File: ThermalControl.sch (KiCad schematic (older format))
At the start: 19 parts, among them U1 ADA4528-2ACPZ-RL, U2 ADA4528-2ACPZ-RL

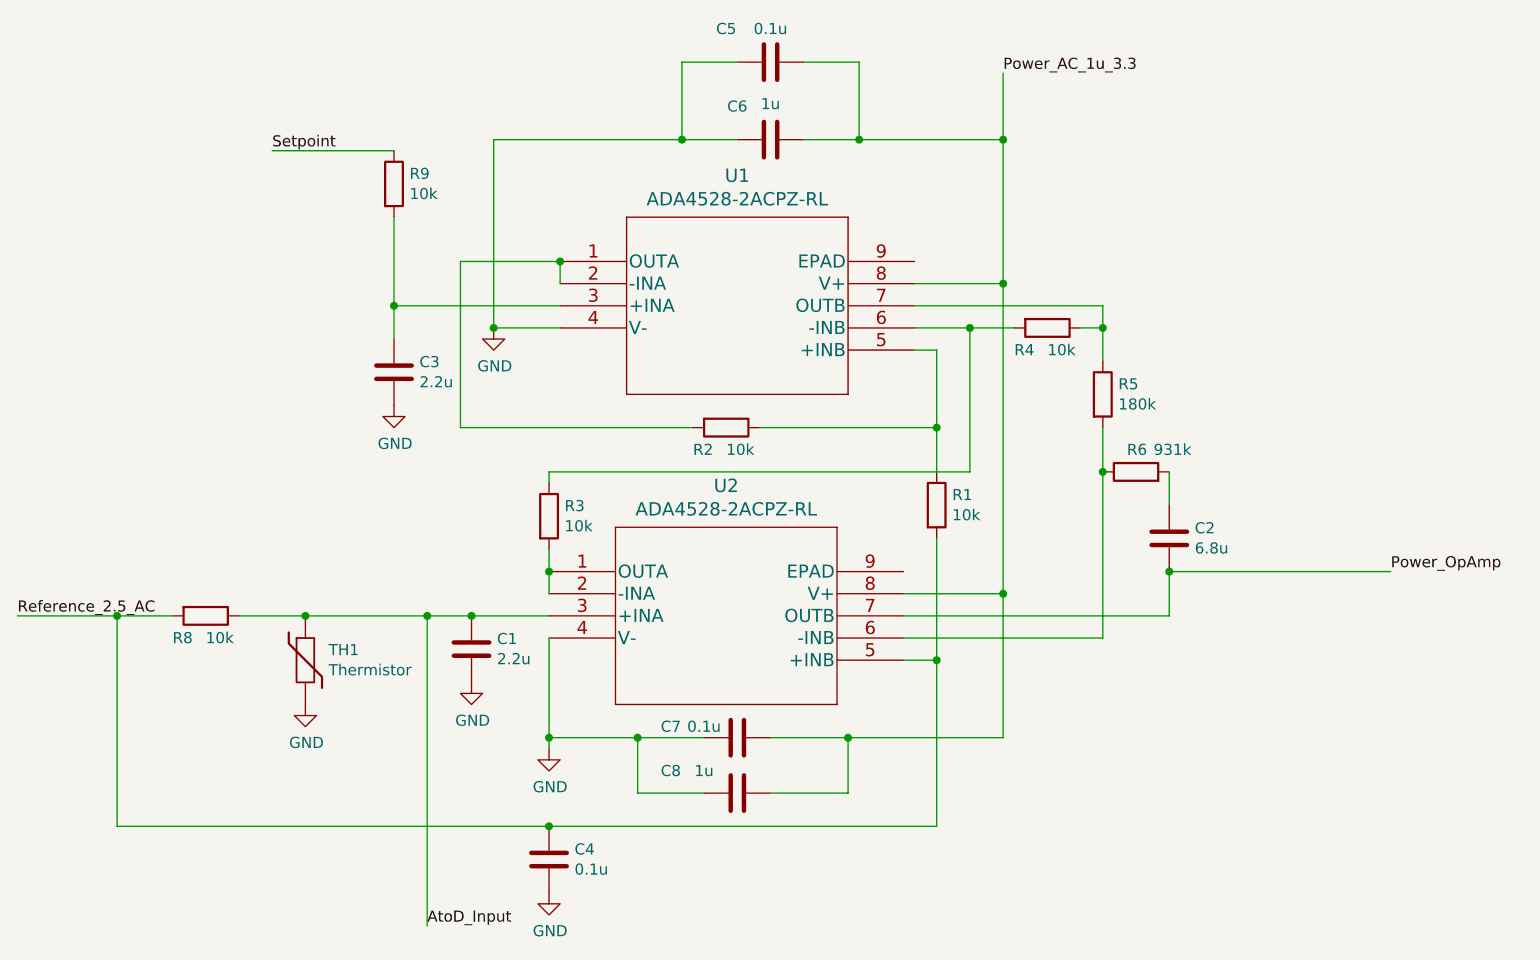
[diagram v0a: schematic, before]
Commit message: annotate all sheets
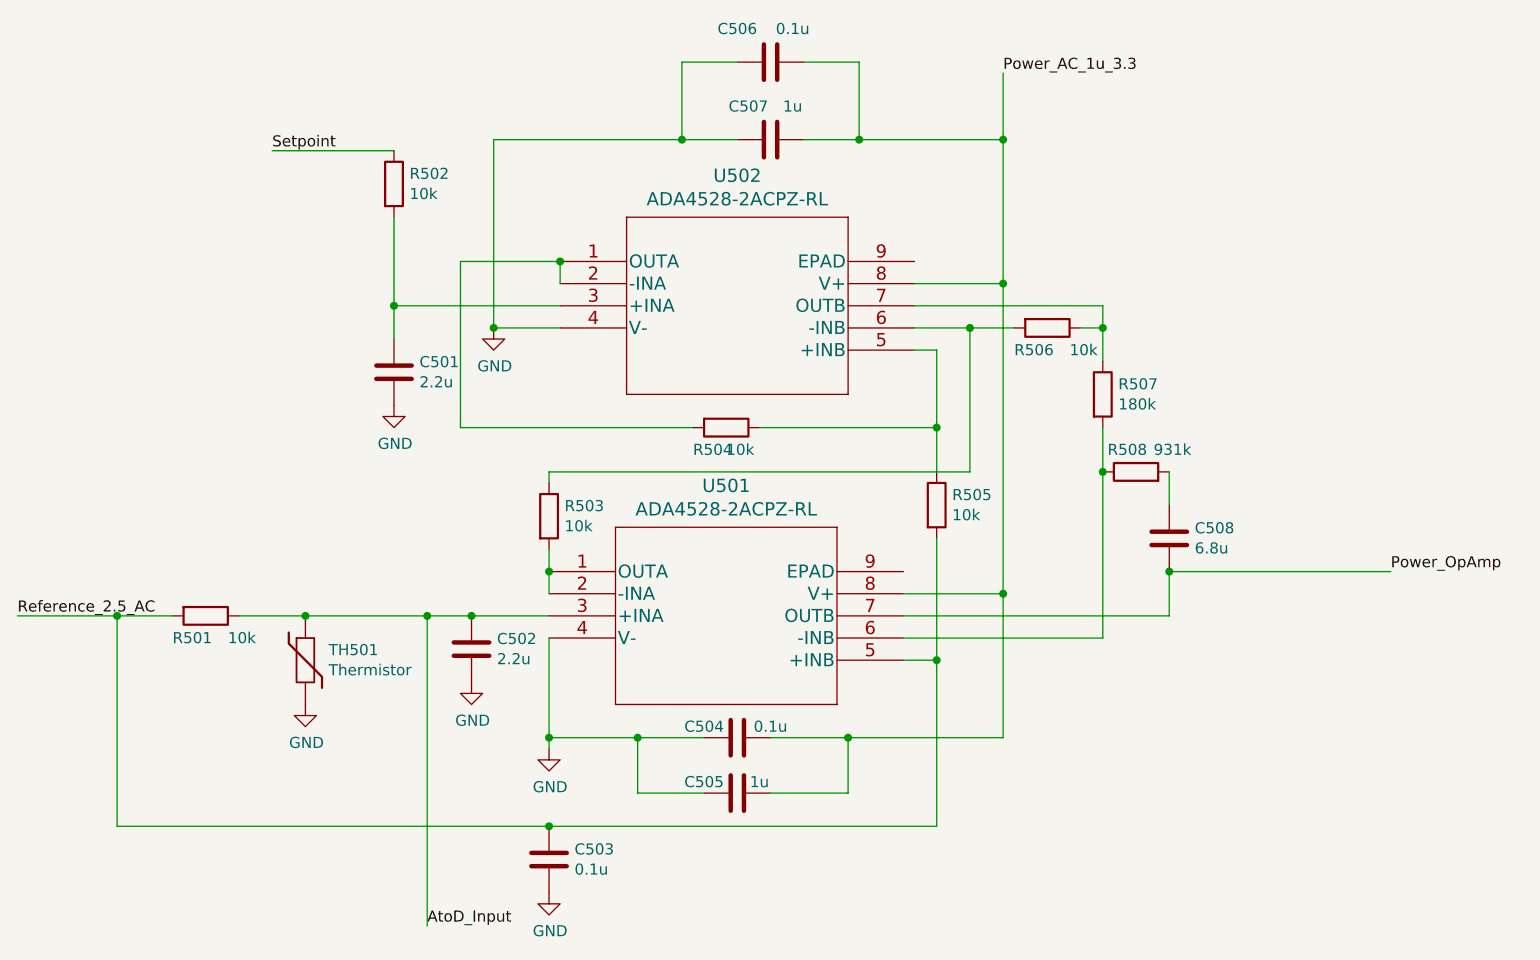
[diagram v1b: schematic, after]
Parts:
- renumbered C3 to C501, C1 to C502, C4 to C503, C7 to C504, C8 to C505, C5 to C506, C6 to C507, C2 to C508, R8 to R501, R9 to R502, R3 to R503, R2 to R504, R1 to R505, R4 to R506, R5 to R507, R6 to R508, TH1 to TH501, U2 to U501, U1 to U502
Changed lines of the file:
@@
 $EndDescr
 $Comp
-L ADA4528-2ACPZ-RL:ADA4528-2ACPZ-RL U2
+L ADA4528-2ACPZ-RL:ADA4528-2ACPZ-RL U501
 U 1 1 60C2B7EB
 P 4800 4550
-F 0 "U2" H 5600 4937 60  0000 C CNN
+F 0 "U501" H 5600 4937 60  0000 C CNN
 F 1 "ADA4528-2ACPZ-RL" H 5600 4831 60  0000 C CNN
 F 2 "CP_8_11_ADI" H 5600 4790 60  0001 C CNN
@@
 $EndComp
 $Comp
-L Device:R R9
+L Device:R R502
 U 1 1 60C2E3AF
 P 4100 2800
-F 0 "R9" H 4170 2846 50  0000 L CNN
+F 0 "R502" H 4170 2846 50  0000 L CNN
 F 1 "10k" H 4170 2755 50  0000 L CNN
 F 2 "" V 4030 2800 50  0001 C CNN
@@
 $EndComp
 $Comp
-L Device:R R4
+L Device:R R506
 U 1 1 60C2E585
 P 7050 3450
-F 0 "R4" V 7150 3300 50  0000 L CNN
-F 1 "10k" V 7150 3450 50  0000 L CNN
+F 0 "R506" V 7150 3300 50  0000 L CNN
+F 1 "10k" V 7150 3550 50  0000 L CNN
 F 2 "" V 6980 3450 50  0001 C CNN
 F 3 "~" H 7050 3450 50  0001 C CNN
@@
 $EndComp
 $Comp
-L Device:R R2
+L Device:R R504
 U 1 1 60C2FA14
 P 5600 3900
-F 0 "R2" V 5700 3750 50  0000 L CNN
+F 0 "R504" V 5700 3750 50  0000 L CNN
 F 1 "10k" V 5700 3900 50  0000 L CNN
 F 2 "" V 5530 3900 50  0001 C CNN
@@
 $EndComp
 $Comp
-L Device:R R5
+L Device:R R507
 U 1 1 60C30AE7
 P 7300 3750
-F 0 "R5" H 7370 3796 50  0000 L CNN
+F 0 "R507" H 7370 3796 50  0000 L CNN
 F 1 "180k" H 7370 3705 50  0000 L CNN
 F 2 "" V 7230 3750 50  0001 C CNN
@@
 $EndComp
 $Comp
-L Device:R R6
+L Device:R R508
 U 1 1 60C314AF
 P 7450 4100
-F 0 "R6" V 7550 4050 50  0000 L CNN
+F 0 "R508" V 7550 4050 50  0000 L CNN
 F 1 "931k" V 7550 3850 50  0000 L CNN
 F 2 "" V 7380 4100 50  0001 C CNN
@@
 $EndComp
 $Comp
-L Device:R R3
+L Device:R R503
 U 1 1 60C32D4C
 P 4800 4300
-F 0 "R3" H 4870 4346 50  0000 L CNN
+F 0 "R503" H 4870 4346 50  0000 L CNN
 F 1 "10k" H 4870 4255 50  0000 L CNN
 F 2 "" V 4730 4300 50  0001 C CNN
@@
 $EndComp
 $Comp
-L Device:R R1
+L Device:R R505
 U 1 1 60C33336
 P 6550 4250
-F 0 "R1" H 6620 4296 50  0000 L CNN
+F 0 "R505" H 6620 4296 50  0000 L CNN
 F 1 "10k" H 6620 4205 50  0000 L CNN
 F 2 "" V 6480 4250 50  0001 C CNN
@@
 $EndComp
 $Comp
-L Device:R R8
+L Device:R R501
 U 1 1 60C33A97
 P 3250 4750
-F 0 "R8" V 3350 4600 50  0000 L CNN
-F 1 "10k" V 3350 4750 50  0000 L CNN
+F 0 "R501" V 3350 4600 50  0000 L CNN
+F 1 "10k" V 3350 4850 50  0000 L CNN
 F 2 "" V 3180 4750 50  0001 C CNN
 F 3 "~" H 3250 4750 50  0001 C CNN
@@
 $EndComp
 $Comp
-L Device:Thermistor TH1
+L Device:Thermistor TH501
 U 1 1 60C34A4A
 P 3700 4950
-F 0 "TH1" H 3805 4996 50  0000 L CNN
+F 0 "TH501" H 3805 4996 50  0000 L CNN
 F 1 "Thermistor" H 3805 4905 50  0000 L CNN
 F 2 "" H 3700 4950 50  0001 C CNN
@@
 $EndComp
 $Comp
-L Device:C C3
+L Device:C C501
 U 1 1 60C35080
 P 4100 3650
-F 0 "C3" H 4215 3696 50  0000 L CNN
+F 0 "C501" H 4215 3696 50  0000 L CNN
 F 1 "2.2u" H 4215 3605 50  0000 L CNN
 F 2 "" H 4138 3500 50  0001 C CNN
@@
 $EndComp
 $Comp
-L Device:C C1
+L Device:C C502
 U 1 1 60C3526E
 P 4450 4900
-F 0 "C1" H 4565 4946 50  0000 L CNN
+F 0 "C502" H 4565 4946 50  0000 L CNN
 F 1 "2.2u" H 4565 4855 50  0000 L CNN
 F 2 "" H 4488 4750 50  0001 C CNN
@@
 $EndComp
 $Comp
-L Device:C C2
+L Device:C C508
 U 1 1 60C3617C
 P 7600 4400
-F 0 "C2" H 7715 4446 50  0000 L CNN
+F 0 "C508" H 7715 4446 50  0000 L CNN
 F 1 "6.8u" H 7715 4355 50  0000 L CNN
 F 2 "" H 7638 4250 50  0001 C CNN
@@
 	4100 3350 4100 3500
 $Comp
-L power:GND #PWR033
+L power:GND #PWR0502
 U 1 1 60C1217C
 P 4100 3800
-F 0 "#PWR033" H 4100 3550 50  0001 C CNN
+F 0 "#PWR0502" H 4100 3550 50  0001 C CNN
 F 1 "GND" H 4105 3627 50  0000 C CNN
 F 2 "" H 4100 3800 50  0001 C CNN
@@
 Connection ~ 7600 4550
 $Comp
-L power:GND #PWR036
+L power:GND #PWR0505
 U 1 1 60C22FFC
 P 4800 5350
-F 0 "#PWR036" H 4800 5100 50  0001 C CNN
+F 0 "#PWR0505" H 4800 5100 50  0001 C CNN
 F 1 "GND" H 4805 5177 50  0000 C CNN
 F 2 "" H 4800 5350 50  0001 C CNN
@@
 	4800 4750 4450 4750
 $Comp
-L power:GND #PWR032
+L power:GND #PWR0501
 U 1 1 60C40715
 P 3700 5150
-F 0 "#PWR032" H 3700 4900 50  0001 C CNN
+F 0 "#PWR0501" H 3700 4900 50  0001 C CNN
 F 1 "GND" H 3705 4977 50  0000 C CNN
 F 2 "" H 3700 5150 50  0001 C CNN
@@
 $EndComp
 $Comp
-L power:GND #PWR034
+L power:GND #PWR0503
 U 1 1 60C40C53
 P 4450 5050
-F 0 "#PWR034" H 4450 4800 50  0001 C CNN
+F 0 "#PWR0503" H 4450 4800 50  0001 C CNN
 F 1 "GND" H 4455 4877 50  0000 C CNN
 F 2 "" H 4450 5050 50  0001 C CNN
@@
 $EndComp
 $Comp
-L power:GND #PWR037
+L power:GND #PWR0506
 U 1 1 60C415D8
 P 4800 6000
-F 0 "#PWR037" H 4800 5750 50  0001 C CNN
+F 0 "#PWR0506" H 4800 5750 50  0001 C CNN
 F 1 "GND" H 4805 5827 50  0000 C CNN
 F 2 "" H 4800 6000 50  0001 C CNN
@@
 $EndComp
 $Comp
-L Device:C C4
+L Device:C C503
 U 1 1 60C41EBD
 P 4800 5850
-F 0 "C4" H 4915 5896 50  0000 L CNN
+F 0 "C503" H 4915 5896 50  0000 L CNN
 F 1 "0.1u" H 4915 5805 50  0000 L CNN
 F 2 "" H 4838 5700 50  0001 C CNN
@@
 	4400 3150 4850 3150
 $Comp
-L ADA4528-2ACPZ-RL:ADA4528-2ACPZ-RL U1
+L ADA4528-2ACPZ-RL:ADA4528-2ACPZ-RL U502
 U 1 1 60C2ACE4
 P 4850 3150
-F 0 "U1" H 5650 3537 60  0000 C CNN
+F 0 "U502" H 5650 3537 60  0000 C CNN
 F 1 "ADA4528-2ACPZ-RL" H 5650 3431 60  0000 C CNN
 F 2 "CP_8_11_ADI" H 5650 3390 60  0001 C CNN
@@
 $EndComp
 $Comp
-L power:GND #PWR035
+L power:GND #PWR0504
 U 1 1 60C13459
 P 4550 3450
-F 0 "#PWR035" H 4550 3200 50  0001 C CNN
+F 0 "#PWR0504" H 4550 3200 50  0001 C CNN
 F 1 "GND" H 4555 3277 50  0000 C CNN
 F 2 "" H 4550 3450 50  0001 C CNN
@@
 Connection ~ 6850 4650
 $Comp
-L Device:C C7
+L Device:C C504
 U 1 1 60C87DF8
 P 5650 5300
-F 0 "C7" V 5600 5000 50  0000 C CNN
-F 1 "0.1u" V 5600 5150 50  0000 C CNN
+F 0 "C504" V 5600 5150 50  0000 C CNN
+F 1 "0.1u" V 5600 5450 50  0000 C CNN
 F 2 "" H 5688 5150 50  0001 C CNN
 F 3 "~" H 5650 5300 50  0001 C CNN
@@
 	5800 5300 6150 5300
 $Comp
-L Device:C C8
+L Device:C C505
 U 1 1 60C88C72
 P 5650 5550
-F 0 "C8" V 5550 5250 50  0000 C CNN
-F 1 "1u" V 5550 5400 50  0000 C CNN
+F 0 "C505" V 5600 5400 50  0000 C CNN
+F 1 "1u" V 5600 5650 50  0000 C CNN
 F 2 "" H 5688 5400 50  0001 C CNN
 F 3 "~" H 5650 5550 50  0001 C CNN
@@
 	5950 2250 6200 2250
 $Comp
-L Device:C C5
+L Device:C C506
 U 1 1 60C7F59C
 P 5800 2250
-F 0 "C5" V 5650 2050 50  0000 C CNN
-F 1 "0.1u" V 5650 2250 50  0000 C CNN
+F 0 "C506" V 5650 2100 50  0000 C CNN
+F 1 "0.1u" V 5650 2350 50  0000 C CNN
 F 2 "" H 5838 2100 50  0001 C CNN
 F 3 "~" H 5800 2250 50  0001 C CNN
@@
 $EndComp
 $Comp
-L Device:C C6
+L Device:C C507
 U 1 1 60C809B8
 P 5800 2600
-F 0 "C6" V 5650 2450 50  0000 C CNN
-F 1 "1u" V 5639 2600 50  0000 C CNN
+F 0 "C507" V 5650 2500 50  0000 C CNN
+F 1 "1u" V 5650 2700 50  0000 C CNN
 F 2 "" H 5838 2450 50  0001 C CNN
 F 3 "~" H 5800 2600 50  0001 C CNN

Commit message: add footprints julia
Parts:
- U501, U502: footprint CP_8_11_ADI -> footprint libraries:ADA4528-2ACPZ-RL
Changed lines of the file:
@@
 F 0 "U501" H 5600 4937 60  0000 C CNN
 F 1 "ADA4528-2ACPZ-RL" H 5600 4831 60  0000 C CNN
-F 2 "CP_8_11_ADI" H 5600 4790 60  0001 C CNN
+F 2 "footprint libraries:ADA4528-2ACPZ-RL" H 5600 4790 60  0001 C CNN
 F 3 "" H 4800 4550 60  0000 C CNN
 	1    4800 4550
@@
 F 0 "U502" H 5650 3537 60  0000 C CNN
 F 1 "ADA4528-2ACPZ-RL" H 5650 3431 60  0000 C CNN
-F 2 "CP_8_11_ADI" H 5650 3390 60  0001 C CNN
+F 2 "footprint libraries:ADA4528-2ACPZ-RL" H 5650 3390 60  0001 C CNN
 F 3 "" H 4850 3150 60  0000 C CNN
 	1    4850 3150

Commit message: added vishay dude & capacitor & resistor footprints
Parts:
- C501, C502, C503, C504, C505, C506, C507, C508: footprint (none) -> Capacitor_SMD:C_0402_1005Metric
- R501, R502, R503, R504, R505, R506, R507, R508: footprint (none) -> Resistor_SMD:R_0402_1005Metric
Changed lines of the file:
@@
 F 0 "R502" H 4170 2846 50  0000 L CNN
 F 1 "10k" H 4170 2755 50  0000 L CNN
-F 2 "" V 4030 2800 50  0001 C CNN
+F 2 "Resistor_SMD:R_0402_1005Metric" V 4030 2800 50  0001 C CNN
 F 3 "~" H 4100 2800 50  0001 C CNN
 	1    4100 2800
@@
 F 0 "R506" V 7150 3300 50  0000 L CNN
 F 1 "10k" V 7150 3550 50  0000 L CNN
-F 2 "" V 6980 3450 50  0001 C CNN
+F 2 "Resistor_SMD:R_0402_1005Metric" V 6980 3450 50  0001 C CNN
 F 3 "~" H 7050 3450 50  0001 C CNN
 	1    7050 3450
@@
 F 0 "R504" V 5700 3750 50  0000 L CNN
 F 1 "10k" V 5700 3900 50  0000 L CNN
-F 2 "" V 5530 3900 50  0001 C CNN
+F 2 "Resistor_SMD:R_0402_1005Metric" V 5530 3900 50  0001 C CNN
 F 3 "~" H 5600 3900 50  0001 C CNN
 	1    5600 3900
@@
 F 0 "R507" H 7370 3796 50  0000 L CNN
 F 1 "180k" H 7370 3705 50  0000 L CNN
-F 2 "" V 7230 3750 50  0001 C CNN
+F 2 "Resistor_SMD:R_0402_1005Metric" V 7230 3750 50  0001 C CNN
 F 3 "~" H 7300 3750 50  0001 C CNN
 	1    7300 3750
@@
 F 0 "R508" V 7550 4050 50  0000 L CNN
 F 1 "931k" V 7550 3850 50  0000 L CNN
-F 2 "" V 7380 4100 50  0001 C CNN
+F 2 "Resistor_SMD:R_0402_1005Metric" V 7380 4100 50  0001 C CNN
 F 3 "~" H 7450 4100 50  0001 C CNN
 	1    7450 4100
@@
 F 0 "R503" H 4870 4346 50  0000 L CNN
 F 1 "10k" H 4870 4255 50  0000 L CNN
-F 2 "" V 4730 4300 50  0001 C CNN
+F 2 "Resistor_SMD:R_0402_1005Metric" V 4730 4300 50  0001 C CNN
 F 3 "~" H 4800 4300 50  0001 C CNN
 	1    4800 4300
@@
 F 0 "R505" H 6620 4296 50  0000 L CNN
 F 1 "10k" H 6620 4205 50  0000 L CNN
-F 2 "" V 6480 4250 50  0001 C CNN
+F 2 "Resistor_SMD:R_0402_1005Metric" V 6480 4250 50  0001 C CNN
 F 3 "~" H 6550 4250 50  0001 C CNN
 	1    6550 4250
@@
 F 0 "R501" V 3350 4600 50  0000 L CNN
 F 1 "10k" V 3350 4850 50  0000 L CNN
-F 2 "" V 3180 4750 50  0001 C CNN
+F 2 "Resistor_SMD:R_0402_1005Metric" V 3180 4750 50  0001 C CNN
 F 3 "~" H 3250 4750 50  0001 C CNN
 	1    3250 4750
@@
 F 0 "C501" H 4215 3696 50  0000 L CNN
 F 1 "2.2u" H 4215 3605 50  0000 L CNN
-F 2 "" H 4138 3500 50  0001 C CNN
+F 2 "Capacitor_SMD:C_0402_1005Metric" H 4138 3500 50  0001 C CNN
 F 3 "~" H 4100 3650 50  0001 C CNN
 	1    4100 3650
@@
 F 0 "C502" H 4565 4946 50  0000 L CNN
 F 1 "2.2u" H 4565 4855 50  0000 L CNN
-F 2 "" H 4488 4750 50  0001 C CNN
+F 2 "Capacitor_SMD:C_0402_1005Metric" H 4488 4750 50  0001 C CNN
 F 3 "~" H 4450 4900 50  0001 C CNN
 	1    4450 4900
@@
 F 0 "C508" H 7715 4446 50  0000 L CNN
 F 1 "6.8u" H 7715 4355 50  0000 L CNN
-F 2 "" H 7638 4250 50  0001 C CNN
+F 2 "Capacitor_SMD:C_0402_1005Metric" H 7638 4250 50  0001 C CNN
 F 3 "~" H 7600 4400 50  0001 C CNN
 	1    7600 4400
@@
 F 0 "C503" H 4915 5896 50  0000 L CNN
 F 1 "0.1u" H 4915 5805 50  0000 L CNN
-F 2 "" H 4838 5700 50  0001 C CNN
+F 2 "Capacitor_SMD:C_0402_1005Metric" H 4838 5700 50  0001 C CNN
 F 3 "~" H 4800 5850 50  0001 C CNN
 	1    4800 5850
@@
 F 0 "C504" V 5600 5150 50  0000 C CNN
 F 1 "0.1u" V 5600 5450 50  0000 C CNN
-F 2 "" H 5688 5150 50  0001 C CNN
+F 2 "Capacitor_SMD:C_0402_1005Metric" H 5688 5150 50  0001 C CNN
 F 3 "~" H 5650 5300 50  0001 C CNN
 	1    5650 5300
@@
 F 0 "C505" V 5600 5400 50  0000 C CNN
 F 1 "1u" V 5600 5650 50  0000 C CNN
-F 2 "" H 5688 5400 50  0001 C CNN
+F 2 "Capacitor_SMD:C_0402_1005Metric" H 5688 5400 50  0001 C CNN
 F 3 "~" H 5650 5550 50  0001 C CNN
 	1    5650 5550
@@
 F 0 "C506" V 5650 2100 50  0000 C CNN
 F 1 "0.1u" V 5650 2350 50  0000 C CNN
-F 2 "" H 5838 2100 50  0001 C CNN
+F 2 "Capacitor_SMD:C_0402_1005Metric" H 5838 2100 50  0001 C CNN
 F 3 "~" H 5800 2250 50  0001 C CNN
 	1    5800 2250
@@
 F 0 "C507" V 5650 2500 50  0000 C CNN
 F 1 "1u" V 5650 2700 50  0000 C CNN
-F 2 "" H 5838 2450 50  0001 C CNN
+F 2 "Capacitor_SMD:C_0402_1005Metric" H 5838 2450 50  0001 C CNN
 F 3 "~" H 5800 2600 50  0001 C CNN
 	1    5800 2600

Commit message: changed all 'odd' resistors in thermal control footprints
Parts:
- C508: footprint Capacitor_SMD:C_0402_1005Metric -> Capacitor_SMD:C_1812_4532Metric
- R501, R502, R503, R504, R505, R506, R507: footprint Resistor_SMD:R_0402_1005Metric -> Resistor_SMD:R_0603_1608Metric
- R508: footprint Resistor_SMD:R_0402_1005Metric -> Resistor_SMD:R_0805_2012Metric
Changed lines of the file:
@@
 F 0 "R502" H 4170 2846 50  0000 L CNN
 F 1 "10k" H 4170 2755 50  0000 L CNN
-F 2 "Resistor_SMD:R_0402_1005Metric" V 4030 2800 50  0001 C CNN
+F 2 "Resistor_SMD:R_0603_1608Metric" V 4030 2800 50  0001 C CNN
 F 3 "~" H 4100 2800 50  0001 C CNN
 	1    4100 2800
@@
 F 0 "R506" V 7150 3300 50  0000 L CNN
 F 1 "10k" V 7150 3550 50  0000 L CNN
-F 2 "Resistor_SMD:R_0402_1005Metric" V 6980 3450 50  0001 C CNN
+F 2 "Resistor_SMD:R_0603_1608Metric" V 6980 3450 50  0001 C CNN
 F 3 "~" H 7050 3450 50  0001 C CNN
 	1    7050 3450
@@
 F 0 "R504" V 5700 3750 50  0000 L CNN
 F 1 "10k" V 5700 3900 50  0000 L CNN
-F 2 "Resistor_SMD:R_0402_1005Metric" V 5530 3900 50  0001 C CNN
+F 2 "Resistor_SMD:R_0603_1608Metric" V 5530 3900 50  0001 C CNN
 F 3 "~" H 5600 3900 50  0001 C CNN
 	1    5600 3900
@@
 F 0 "R507" H 7370 3796 50  0000 L CNN
 F 1 "180k" H 7370 3705 50  0000 L CNN
-F 2 "Resistor_SMD:R_0402_1005Metric" V 7230 3750 50  0001 C CNN
+F 2 "Resistor_SMD:R_0603_1608Metric" V 7230 3750 50  0001 C CNN
 F 3 "~" H 7300 3750 50  0001 C CNN
 	1    7300 3750
@@
 F 0 "R508" V 7550 4050 50  0000 L CNN
 F 1 "931k" V 7550 3850 50  0000 L CNN
-F 2 "Resistor_SMD:R_0402_1005Metric" V 7380 4100 50  0001 C CNN
+F 2 "Resistor_SMD:R_0805_2012Metric" V 7380 4100 50  0001 C CNN
 F 3 "~" H 7450 4100 50  0001 C CNN
 	1    7450 4100
@@
 F 0 "R503" H 4870 4346 50  0000 L CNN
 F 1 "10k" H 4870 4255 50  0000 L CNN
-F 2 "Resistor_SMD:R_0402_1005Metric" V 4730 4300 50  0001 C CNN
+F 2 "Resistor_SMD:R_0603_1608Metric" V 4730 4300 50  0001 C CNN
 F 3 "~" H 4800 4300 50  0001 C CNN
 	1    4800 4300
@@
 F 0 "R505" H 6620 4296 50  0000 L CNN
 F 1 "10k" H 6620 4205 50  0000 L CNN
-F 2 "Resistor_SMD:R_0402_1005Metric" V 6480 4250 50  0001 C CNN
+F 2 "Resistor_SMD:R_0603_1608Metric" V 6480 4250 50  0001 C CNN
 F 3 "~" H 6550 4250 50  0001 C CNN
 	1    6550 4250
@@
 F 0 "R501" V 3350 4600 50  0000 L CNN
 F 1 "10k" V 3350 4850 50  0000 L CNN
-F 2 "Resistor_SMD:R_0402_1005Metric" V 3180 4750 50  0001 C CNN
+F 2 "Resistor_SMD:R_0603_1608Metric" V 3180 4750 50  0001 C CNN
 F 3 "~" H 3250 4750 50  0001 C CNN
 	1    3250 4750
@@
 F 0 "C508" H 7715 4446 50  0000 L CNN
 F 1 "6.8u" H 7715 4355 50  0000 L CNN
-F 2 "Capacitor_SMD:C_0402_1005Metric" H 7638 4250 50  0001 C CNN
+F 2 "Capacitor_SMD:C_1812_4532Metric" H 7638 4250 50  0001 C CNN
 F 3 "~" H 7600 4400 50  0001 C CNN
 	1    7600 4400
